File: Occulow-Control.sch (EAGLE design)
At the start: 45 parts, among them T1 DMP3010LK3, T2 DMP3010LK3, T3 DMP3010LK3

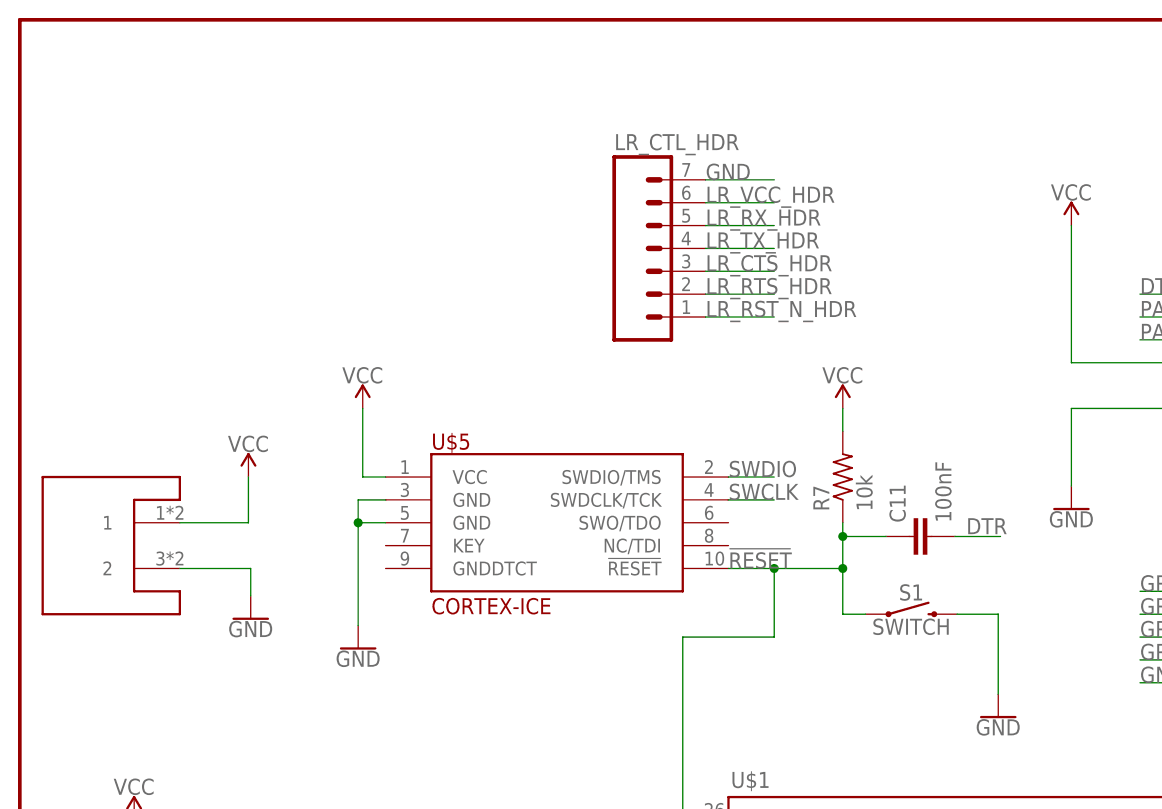
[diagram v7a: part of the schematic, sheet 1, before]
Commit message: Added lib for ldo voltage regulator, placed in schematic. No layout
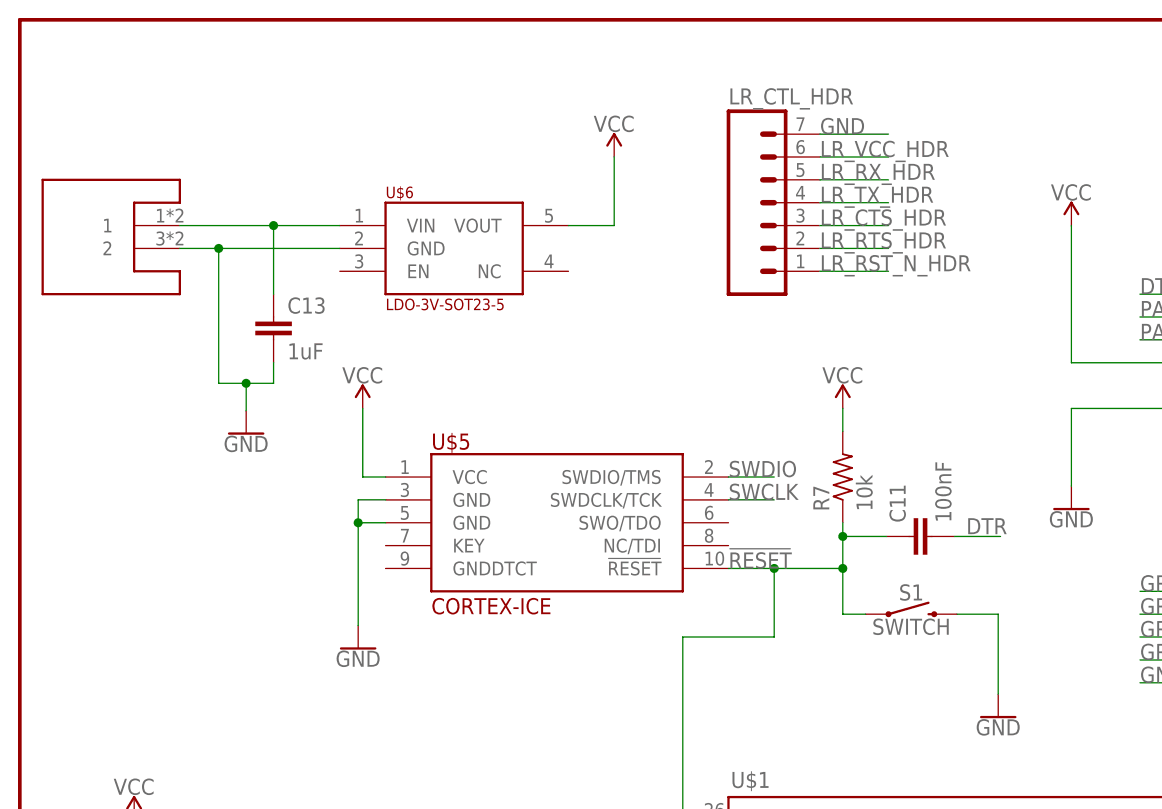
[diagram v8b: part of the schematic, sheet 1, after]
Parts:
- added C13: 1uF, rcl:C-EUC1206
- added U$6: LDO-3V-SOT23-5, Occulow:LDO-3V-SOT23-5
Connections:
- new net N$5: C13.1, U$6.VIN, U$7.1
- net GND: now also C13.2, U$6.GND
- net VCC: now also U$6.VOUT; no longer U$7.1
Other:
- moved on the sheet: LR_CTL_HDR
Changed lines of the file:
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@@
 <part name="I2C_HDR" library="con-amp-quick" deviceset="M02" device=""/>
 <part name="U$7" library="lite-trap" deviceset="MINI-LITE-TRAP" device=""/>
+<part name="U$6" library="Occulow" deviceset="LDO-3V-SOT23-5" device=""/>
+<part name="C13" library="rcl" deviceset="C-EU" device="C1206" value="1uF"/>
 </parts>
 <sheets>
@@
 <instance part="SUPPLY5" gate="G$1" x="116.84" y="162.56"/>
 <instance part="GND10" gate="1" x="116.84" y="131.064"/>
-<instance part="SUPPLY6" gate="G$1" x="25.4" y="134.62"/>
-<instance part="GND11" gate="1" x="25.654" y="118.872"/>
+<instance part="SUPPLY6" gate="G$1" x="66.04" y="170.18"/>
+<instance part="GND11" gate="1" x="25.146" y="139.446"/>
 <instance part="L1" gate="G$1" x="66.04" y="81.28" rot="R270"/>
 <instance part="L2" gate="G$1" x="17.78" y="91.44" rot="R270"/>
@@
 <instance part="H2" gate="G$1" x="40.64" y="5.08"/>
 <instance part="H3" gate="G$1" x="45.72" y="5.08"/>
-<instance part="LR_CTL_HDR" gate="G$1" x="71.12" y="157.48"/>
+<instance part="LR_CTL_HDR" gate="G$1" x="83.82" y="162.56"/>
 <instance part="U$5" gate="G$1" x="58.42" y="129.54"/>
 <instance part="D1" gate="G$1" x="195.58" y="68.58"/>
@@
 <instance part="C11" gate="G$1" x="98.806" y="128.016" rot="R90"/>
 <instance part="I2C_HDR" gate="G$1" x="144.78" y="172.72" rot="R180"/>
-<instance part="U$7" gate="G$1" x="10.16" y="127"/>
+<instance part="U$7" gate="G$1" x="10.16" y="160.02"/>
+<instance part="U$6" gate="G$1" x="48.26" y="160.02"/>
+<instance part="C13" gate="G$1" x="28.194" y="152.4"/>
 </instances>
 <busses>
@@
 <segment>
 <pinref part="LR_CTL_HDR" gate="G$1" pin="7"/>
-<wire x1="76.2" y1="167.64" x2="83.82" y2="167.64" width="0.1524" layer="91"/>
-<label x="76.2" y="167.64" size="1.778" layer="95"/>
+<wire x1="88.9" y1="172.72" x2="96.52" y2="172.72" width="0.1524" layer="91"/>
+<label x="88.9" y="172.72" size="1.778" layer="95"/>
 </segment>
 <segment>
@@
 </segment>
 <segment>
+<pinref part="C13" gate="G$1" pin="2"/>
+<wire x1="28.194" y1="147.32" x2="28.194" y2="145.034" width="0.1524" layer="91"/>
+<wire x1="28.194" y1="145.034" x2="25.146" y2="145.034" width="0.1524" layer="91"/>
+<pinref part="GND11" gate="1" pin="GND"/>
+<wire x1="25.146" y1="141.986" x2="25.146" y2="145.034" width="0.1524" layer="91"/>
 <pinref part="U$7" gate="G$1" pin="2"/>
-<pinref part="GND11" gate="1" pin="GND"/>
-<wire x1="17.78" y1="124.46" x2="25.654" y2="124.46" width="0.1524" layer="91"/>
-<wire x1="25.654" y1="124.46" x2="25.654" y2="121.412" width="0.1524" layer="91"/>
+<pinref part="U$6" gate="G$1" pin="GND"/>
+<wire x1="35.56" y1="160.02" x2="22.098" y2="160.02" width="0.1524" layer="91"/>
+<wire x1="22.098" y1="160.02" x2="17.78" y2="160.02" width="0.1524" layer="91"/>
+<wire x1="25.146" y1="145.034" x2="22.098" y2="145.034" width="0.1524" layer="91"/>
+<wire x1="22.098" y1="145.034" x2="22.098" y2="160.02" width="0.1524" layer="91"/>
+<junction x="25.146" y="145.034"/>
+<junction x="22.098" y="160.02"/>
 </segment>
 </net>
@@
 </segment>
 <segment>
-<pinref part="U$7" gate="G$1" pin="1"/>
+<pinref part="U$6" gate="G$1" pin="VOUT"/>
 <pinref part="SUPPLY6" gate="G$1" pin="VCC"/>
-<wire x1="17.78" y1="129.54" x2="25.4" y2="129.54" width="0.1524" layer="91"/>
-<wire x1="25.4" y1="129.54" x2="25.4" y2="134.62" width="0.1524" layer="91"/>
+<wire x1="60.96" y1="162.56" x2="66.04" y2="162.56" width="0.1524" layer="91"/>
+<wire x1="66.04" y1="162.56" x2="66.04" y2="170.18" width="0.1524" layer="91"/>
 </segment>
 </net>
@@
 <segment>
 <pinref part="LR_CTL_HDR" gate="G$1" pin="5"/>
-<wire x1="76.2" y1="162.56" x2="83.82" y2="162.56" width="0.1524" layer="91"/>
-<label x="76.2" y="162.56" size="1.778" layer="95"/>
+<wire x1="88.9" y1="167.64" x2="96.52" y2="167.64" width="0.1524" layer="91"/>
+<label x="88.9" y="167.64" size="1.778" layer="95"/>
 </segment>
 </net>
@@
 <segment>
 <pinref part="LR_CTL_HDR" gate="G$1" pin="4"/>
-<wire x1="76.2" y1="160.02" x2="83.82" y2="160.02" width="0.1524" layer="91"/>
-<label x="76.2" y="160.02" size="1.778" layer="95"/>
+<wire x1="88.9" y1="165.1" x2="96.52" y2="165.1" width="0.1524" layer="91"/>
+<label x="88.9" y="165.1" size="1.778" layer="95"/>
 </segment>
 </net>
@@
 <segment>
 <pinref part="LR_CTL_HDR" gate="G$1" pin="3"/>
-<wire x1="76.2" y1="157.48" x2="83.82" y2="157.48" width="0.1524" layer="91"/>
-<label x="76.2" y="157.48" size="1.778" layer="95"/>
+<wire x1="88.9" y1="162.56" x2="96.52" y2="162.56" width="0.1524" layer="91"/>
+<label x="88.9" y="162.56" size="1.778" layer="95"/>
 </segment>
 </net>
@@
 <segment>
 <pinref part="LR_CTL_HDR" gate="G$1" pin="2"/>
-<wire x1="76.2" y1="154.94" x2="83.82" y2="154.94" width="0.1524" layer="91"/>
-<label x="76.2" y="154.94" size="1.778" layer="95"/>
+<wire x1="88.9" y1="160.02" x2="96.52" y2="160.02" width="0.1524" layer="91"/>
+<label x="88.9" y="160.02" size="1.778" layer="95"/>
 </segment>
 </net>
@@
 <segment>
 <pinref part="LR_CTL_HDR" gate="G$1" pin="1"/>
-<wire x1="76.2" y1="152.4" x2="83.82" y2="152.4" width="0.1524" layer="91"/>
-<label x="76.2" y="152.4" size="1.778" layer="95"/>
+<wire x1="88.9" y1="157.48" x2="96.52" y2="157.48" width="0.1524" layer="91"/>
+<label x="88.9" y="157.48" size="1.778" layer="95"/>
 </segment>
 </net>
@@
 <segment>
 <pinref part="LR_CTL_HDR" gate="G$1" pin="6"/>
-<wire x1="76.2" y1="165.1" x2="83.82" y2="165.1" width="0.1524" layer="91"/>
-<label x="76.2" y="165.1" size="1.778" layer="95"/>
+<wire x1="88.9" y1="170.18" x2="96.52" y2="170.18" width="0.1524" layer="91"/>
+<label x="88.9" y="170.18" size="1.778" layer="95"/>
 </segment>
 </net>
@@
 </segment>
 </net>
+<net name="N$5" class="0">
+<segment>
+<pinref part="U$7" gate="G$1" pin="1"/>
+<pinref part="U$6" gate="G$1" pin="VIN"/>
+<wire x1="35.56" y1="162.56" x2="28.194" y2="162.56" width="0.1524" layer="91"/>
+<pinref part="C13" gate="G$1" pin="1"/>
+<wire x1="28.194" y1="162.56" x2="17.78" y2="162.56" width="0.1524" layer="91"/>
+<wire x1="28.194" y1="154.94" x2="28.194" y2="162.56" width="0.1524" layer="91"/>
+<junction x="28.194" y="162.56"/>
+</segment>
+</net>
